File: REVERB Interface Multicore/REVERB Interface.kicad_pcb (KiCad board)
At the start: 2 copper layers, 90.2 x 95.9 mm, 71 parts, among them J1 RPiZeroW, J2 Iridium, J3 APRS, J4 Antenna, J5 UPDI, M1 MountingHole_Pad, M2 MountingHole_Pad, M3 MountingHole_Pad, M4 MountingHole_Pad, M5 PiMount, M6 PiMount, M7 PiMount, M8 PiMount, U1 IMU, U2 MAX3232, U3 ATtiny1604-SS, U4 TXB0104D, U5 DS3231BOB, U6 LM1117-3.3

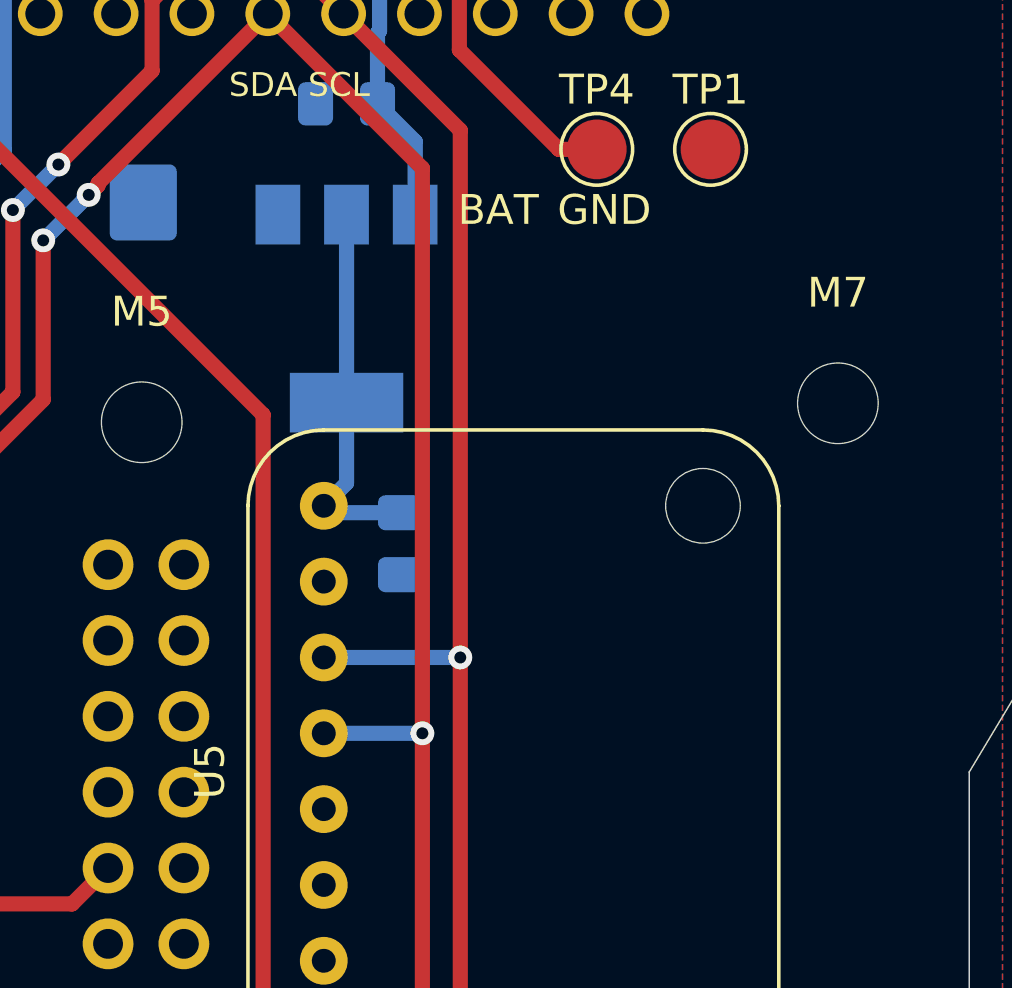
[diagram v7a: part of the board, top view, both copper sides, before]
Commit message: embed the rtc
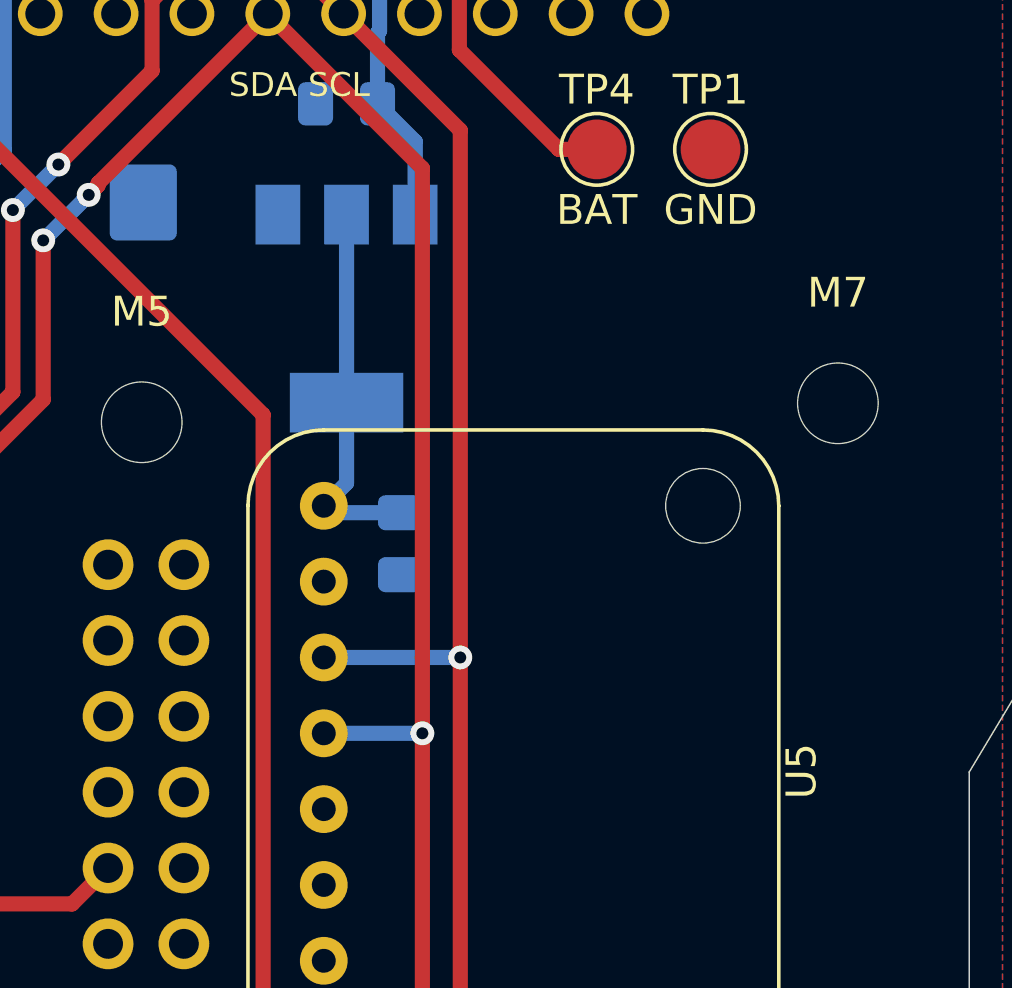
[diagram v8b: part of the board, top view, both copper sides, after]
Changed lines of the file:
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@@
   )
   (setup
-    (last_trace_width 0.508)
+    (last_trace_width 0.25)
     (user_trace_width 0.254)
     (user_trace_width 0.381)
@@
     (add_net +3V3)
     (add_net +5V)
-    (add_net /5VUSBCHG)
     (add_net /APRSRX)
     (add_net /APRSRXSh)
@@
     (add_net /HWTX)
     (add_net /IMURST)
-    (add_net /OE)
     (add_net /PCM_IN)
     (add_net /R1IN)
@@
     (add_net /SLVRST)
     (add_net /SPICE0)
-    (add_net /SPICE1)
     (add_net /SPIMISO)
     (add_net /SPIMOSI)
@@
     (add_net /SPIUARTRX)
     (add_net /SPIUARTTX)
-    (add_net /SW1)
     (add_net /SW10)
-    (add_net /SW2)
     (add_net /SW3)
     (add_net /SW4)
-    (add_net /SW5)
     (add_net /SW6)
     (add_net /SW7)
@@
     (add_net "Net-(D6-Pad2)")
     (add_net "Net-(D9-Pad2)")
-    (add_net "Net-(H1-Pad1)")
-    (add_net "Net-(H1-Pad10)")
-    (add_net "Net-(H1-Pad11)")
-    (add_net "Net-(H1-Pad12)")
-    (add_net "Net-(H1-Pad13)")
-    (add_net "Net-(H1-Pad14)")
-    (add_net "Net-(H1-Pad15)")
-    (add_net "Net-(H1-Pad16)")
-    (add_net "Net-(H1-Pad17)")
-    (add_net "Net-(H1-Pad18)")
-    (add_net "Net-(H1-Pad19)")
-    (add_net "Net-(H1-Pad2)")
-    (add_net "Net-(H1-Pad20)")
-    (add_net "Net-(H1-Pad21)")
-    (add_net "Net-(H1-Pad22)")
-    (add_net "Net-(H1-Pad23)")
-    (add_net "Net-(H1-Pad24)")
-    (add_net "Net-(H1-Pad25)")
-    (add_net "Net-(H1-Pad26)")
-    (add_net "Net-(H1-Pad27)")
-    (add_net "Net-(H1-Pad28)")
-    (add_net "Net-(H1-Pad29)")
-    (add_net "Net-(H1-Pad3)")
-    (add_net "Net-(H1-Pad30)")
-    (add_net "Net-(H1-Pad31)")
-    (add_net "Net-(H1-Pad33)")
-    (add_net "Net-(H1-Pad34)")
-    (add_net "Net-(H1-Pad35)")
-    (add_net "Net-(H1-Pad36)")
-    (add_net "Net-(H1-Pad37)")
-    (add_net "Net-(H1-Pad38)")
-    (add_net "Net-(H1-Pad39)")
-    (add_net "Net-(H1-Pad4)")
-    (add_net "Net-(H1-Pad40)")
-    (add_net "Net-(H1-Pad42)")
-    (add_net "Net-(H1-Pad44)")
-    (add_net "Net-(H1-Pad45)")
-    (add_net "Net-(H1-Pad46)")
-    (add_net "Net-(H1-Pad47)")
-    (add_net "Net-(H1-Pad48)")
-    (add_net "Net-(H1-Pad49)")
-    (add_net "Net-(H1-Pad5)")
-    (add_net "Net-(H1-Pad50)")
-    (add_net "Net-(H1-Pad51)")
-    (add_net "Net-(H1-Pad52)")
-    (add_net "Net-(H1-Pad6)")
-    (add_net "Net-(H1-Pad7)")
-    (add_net "Net-(H1-Pad8)")
-    (add_net "Net-(H1-Pad9)")
-    (add_net "Net-(H2-Pad1)")
-    (add_net "Net-(H2-Pad2)")
-    (add_net "Net-(H2-Pad3)")
-    (add_net "Net-(H2-Pad31)")
-    (add_net "Net-(H2-Pad33)")
-    (add_net "Net-(H2-Pad34)")
-    (add_net "Net-(H2-Pad37)")
-    (add_net "Net-(H2-Pad38)")
-    (add_net "Net-(H2-Pad39)")
-    (add_net "Net-(H2-Pad4)")
-    (add_net "Net-(H2-Pad40)")
-    (add_net "Net-(H2-Pad49)")
-    (add_net "Net-(H2-Pad5)")
-    (add_net "Net-(H2-Pad50)")
-    (add_net "Net-(H2-Pad51)")
-    (add_net "Net-(H2-Pad52)")
-    (add_net "Net-(H2-Pad6)")
-    (add_net "Net-(H2-Pad7)")
-    (add_net "Net-(J1-Pad1)")
-    (add_net "Net-(J1-Pad11)")
-    (add_net "Net-(J1-Pad13)")
-    (add_net "Net-(J1-Pad15)")
-    (add_net "Net-(J1-Pad17)")
-    (add_net "Net-(J1-Pad27)")
-    (add_net "Net-(J1-Pad28)")
-    (add_net "Net-(J1-Pad29)")
-    (add_net "Net-(J1-Pad31)")
-    (add_net "Net-(J1-Pad33)")
-    (add_net "Net-(J1-Pad35)")
-    (add_net "Net-(J1-Pad36)")
-    (add_net "Net-(J1-Pad37)")
-    (add_net "Net-(J1-Pad38)")
-    (add_net "Net-(J1-Pad40)")
-    (add_net "Net-(J1-Pad7)")
-    (add_net "Net-(J2-Pad1)")
-    (add_net "Net-(J2-Pad10)")
-    (add_net "Net-(J2-Pad12)")
-    (add_net "Net-(J2-Pad14)")
-    (add_net "Net-(J2-Pad16)")
-    (add_net "Net-(J2-Pad2)")
-    (add_net "Net-(J2-Pad4)")
-    (add_net "Net-(J2-Pad6)")
-    (add_net "Net-(J2-Pad7)")
-    (add_net "Net-(J2-Pad9)")
-    (add_net "Net-(J3-Pad1)")
-    (add_net "Net-(J3-Pad10)")
-    (add_net "Net-(J3-Pad11)")
-    (add_net "Net-(J3-Pad12)")
-    (add_net "Net-(J3-Pad13)")
-    (add_net "Net-(J3-Pad14)")
-    (add_net "Net-(J3-Pad15)")
-    (add_net "Net-(J3-Pad17)")
-    (add_net "Net-(J3-Pad19)")
-    (add_net "Net-(J3-Pad2)")
-    (add_net "Net-(J3-Pad20)")
-    (add_net "Net-(J3-Pad3)")
-    (add_net "Net-(J3-Pad5)")
-    (add_net "Net-(J3-Pad7)")
-    (add_net "Net-(J3-Pad8)")
-    (add_net "Net-(J3-Pad9)")
     (add_net "Net-(J5-Pad1)")
-    (add_net "Net-(U1-Pad2)")
-    (add_net "Net-(U2-Pad10)")
-    (add_net "Net-(U2-Pad7)")
-    (add_net "Net-(U2-Pad8)")
-    (add_net "Net-(U2-Pad9)")
-    (add_net "Net-(U3-Pad3)")
-    (add_net "Net-(U3-Pad4)")
-    (add_net "Net-(U3-Pad5)")
-    (add_net "Net-(U4-Pad10)")
-    (add_net "Net-(U4-Pad11)")
-    (add_net "Net-(U4-Pad4)")
-    (add_net "Net-(U4-Pad5)")
-    (add_net "Net-(U4-Pad6)")
-    (add_net "Net-(U4-Pad9)")
-    (add_net "Net-(U5-Pad5)")
-    (add_net "Net-(U5-Pad6)")
-    (add_net "Net-(U5-Pad7)")
-    (add_net "Net-(U5-Pad8)")
     (add_net VBUS)
   )
@@
   (module "REVERB Interface:DS3231BOB" (layer F.Cu)
     (at 173.482 90.932 270)
-    (fp_text reference U5 (at 0 3.81 90) (layer F.SilkS)
+    (fp_text reference U5 (at 0 -16.002 90) (layer F.SilkS)
       (effects (font (size 1 1) (thickness 0.15)))
     )
@@
     (effects (font (size 1 1) (thickness 0.15)))
   )
-  (gr_text GND (at 182.88 72.136) (layer F.SilkS)
+  (gr_text GND (at 186.436 72.136) (layer F.SilkS)
     (effects (font (size 1 1) (thickness 0.15)))
   )
-  (gr_text BAT (at 179.324 72.136) (layer F.SilkS)
+  (gr_text BAT (at 182.626 72.136) (layer F.SilkS)
     (effects (font (size 1 1) (thickness 0.15)))
   )
@@
   (segment (start 179.07 124.308) (end 179.172 124.206) (width 0.762) (layer B.Cu) (net 15))
   (segment (start 179.07 129.794) (end 179.07 124.308) (width 0.762) (layer B.Cu) (net 15))
+  (segment (start 168.121 134.139) (end 169.590106 134.139) (width 0.508) (layer F.Cu) (net 15))
+  (segment (start 172.157106 131.572) (end 171.45 131.572) (width 0.508) (layer B.Cu) (net 15))
+  (segment (start 156.811923 64.223001) (end 157.701999 65.113077) (width 0.508) (layer F.Cu) (net 15))
+  (segment (start 171.45 132.279106) (end 171.45 131.572) (width 0.508) (layer F.Cu) (net 15))
+  (segment (start 153.248079 64.223001) (end 156.811923 64.223001) (width 0.508) (layer F.Cu) (net 15))
+  (segment (start 152.621999 61.814999) (end 152.621999 63.596921) (width 0.508) (layer F.Cu) (net 15))
+  (segment (start 177.663 131.572) (end 172.157106 131.572) (width 0.508) (layer B.Cu) (net 15))
+  (segment (start 157.701999 66.136921) (end 159.129078 67.564) (width 0.508) (layer F.Cu) (net 15))
+  (segment (start 160.02 67.564) (end 171.45 78.994) (width 0.508) (layer F.Cu) (net 15))
+  (segment (start 171.45 78.994) (end 171.45 131.572) (width 0.508) (layer F.Cu) (net 15))
+  (segment (start 151.286 60.479) (end 152.621999 61.814999) (width 0.508) (layer F.Cu) (net 15))
+  (segment (start 159.129078 67.564) (end 160.02 67.564) (width 0.508) (layer F.Cu) (net 15))
+  (via (at 171.45 131.572) (size 1) (drill 0.5) (layers F.Cu B.Cu) (net 15))
+  (segment (start 166.256 132.274) (end 168.121 134.139) (width 0.508) (layer F.Cu) (net 15))
+  (segment (start 179.06 130.175) (end 177.663 131.572) (width 0.508) (layer B.Cu) (net 15))
+  (segment (start 157.701999 65.113077) (end 157.701999 66.136921) (width 0.508) (layer F.Cu) (net 15))
+  (segment (start 169.590106 134.139) (end 171.45 132.279106) (width 0.508) (layer F.Cu) (net 15))
+  (segment (start 152.621999 63.596921) (end 153.248079 64.223001) (width 0.508) (layer F.Cu) (net 15))
   (segment (start 148.746 57.939) (end 148.746 60.479) (width 0.508) (layer F.Cu) (net 16))
   (segment (start 147.541999 68.866001) (end 145.796 70.612) (width 0.508) (layer F.Cu) (net 16))
@@
   (segment (start 151.564 132.588) (end 150.984001 132.008001) (width 0.381) (layer F.Cu) (net 37))
   (segment (start 152.719 132.588) (end 151.564 132.588) (width 0.381) (layer F.Cu) (net 37))
-  (segment (start 168.121 134.139) (end 169.590106 134.139) (width 0.508) (layer F.Cu) (net 15))
-  (segment (start 172.157106 131.572) (end 171.45 131.572) (width 0.508) (layer B.Cu) (net 15))
-  (segment (start 156.811923 64.223001) (end 157.701999 65.113077) (width 0.508) (layer F.Cu) (net 15))
-  (segment (start 171.45 132.279106) (end 171.45 131.572) (width 0.508) (layer F.Cu) (net 15))
-  (segment (start 153.248079 64.223001) (end 156.811923 64.223001) (width 0.508) (layer F.Cu) (net 15))
-  (segment (start 152.621999 61.814999) (end 152.621999 63.596921) (width 0.508) (layer F.Cu) (net 15))
-  (segment (start 177.663 131.572) (end 172.157106 131.572) (width 0.508) (layer B.Cu) (net 15))
-  (segment (start 157.701999 66.136921) (end 159.129078 67.564) (width 0.508) (layer F.Cu) (net 15))
-  (segment (start 160.02 67.564) (end 171.45 78.994) (width 0.508) (layer F.Cu) (net 15))
-  (segment (start 171.45 78.994) (end 171.45 131.572) (width 0.508) (layer F.Cu) (net 15))
-  (segment (start 151.286 60.479) (end 152.621999 61.814999) (width 0.508) (layer F.Cu) (net 15))
-  (segment (start 159.129078 67.564) (end 160.02 67.564) (width 0.508) (layer F.Cu) (net 15))
-  (via (at 171.45 131.572) (size 1) (drill 0.5) (layers F.Cu B.Cu) (net 15))
-  (segment (start 166.256 132.274) (end 168.121 134.139) (width 0.508) (layer F.Cu) (net 15))
-  (segment (start 179.06 130.175) (end 177.663 131.572) (width 0.508) (layer B.Cu) (net 15))
-  (segment (start 157.701999 65.113077) (end 157.701999 66.136921) (width 0.508) (layer F.Cu) (net 15))
-  (segment (start 169.590106 134.139) (end 171.45 132.279106) (width 0.508) (layer F.Cu) (net 15))
-  (segment (start 152.621999 63.596921) (end 153.248079 64.223001) (width 0.508) (layer F.Cu) (net 15))
   (via (at 179.324 102.997) (size 0.8) (drill 0.4) (layers F.Cu B.Cu) (net 38))
   (segment (start 167.555499 103.034501) (end 179.286499 103.034501) (width 0.381) (layer B.Cu) (net 38))
